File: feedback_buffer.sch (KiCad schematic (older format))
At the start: 20 parts

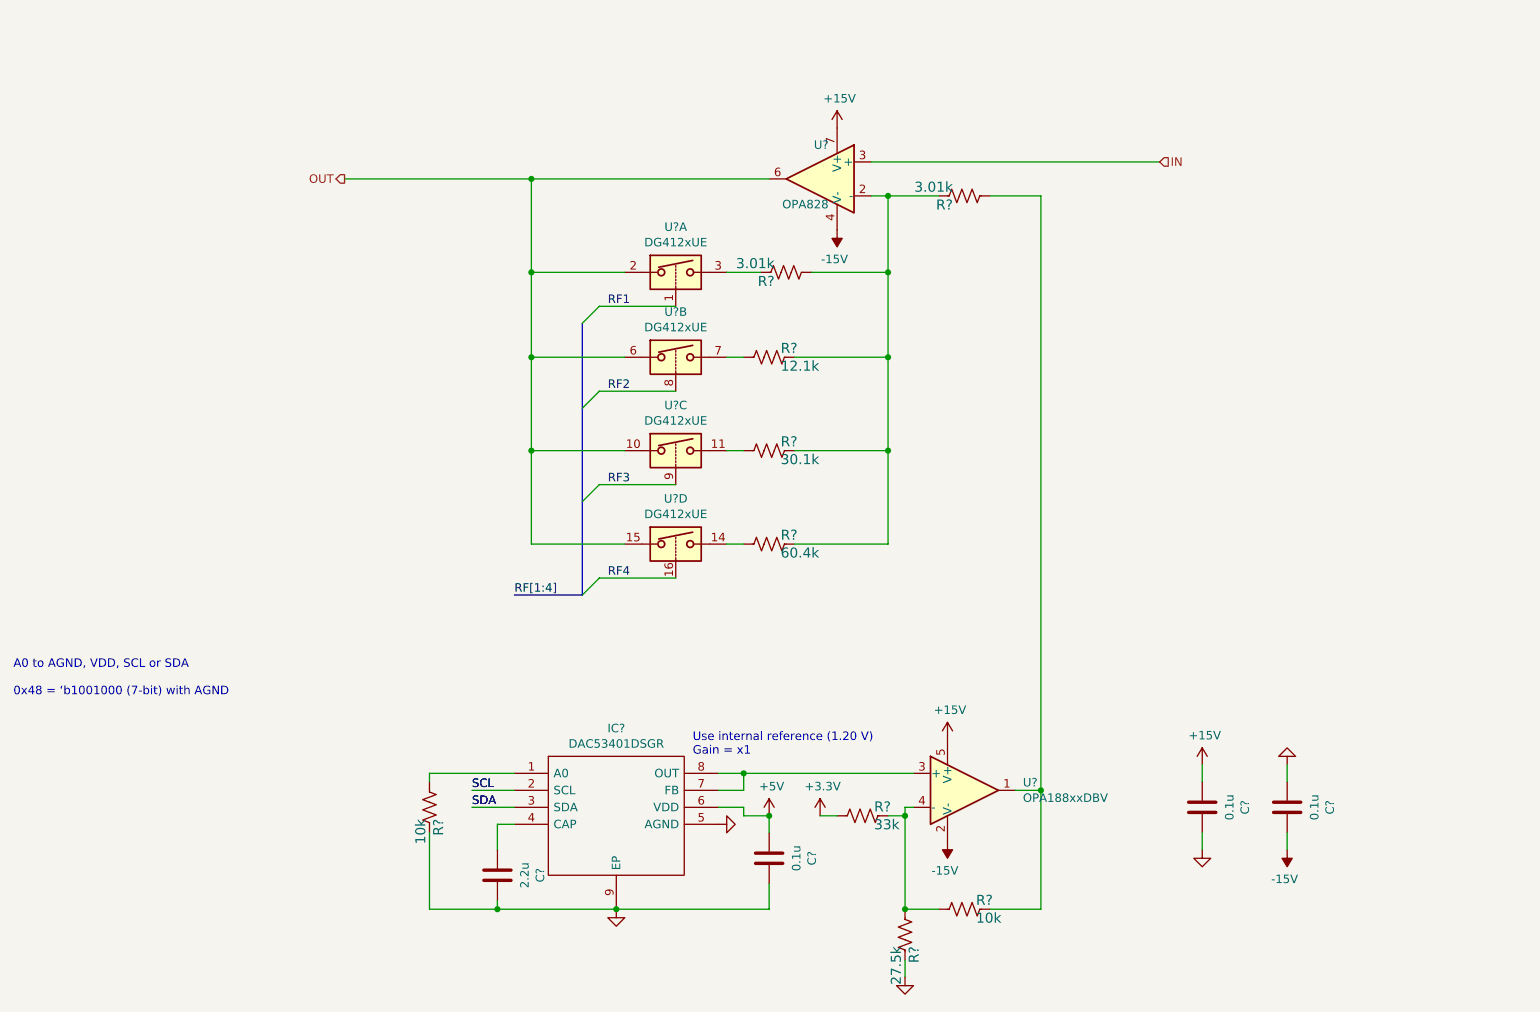
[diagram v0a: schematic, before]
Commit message: reduced ERC to just 4 warnings
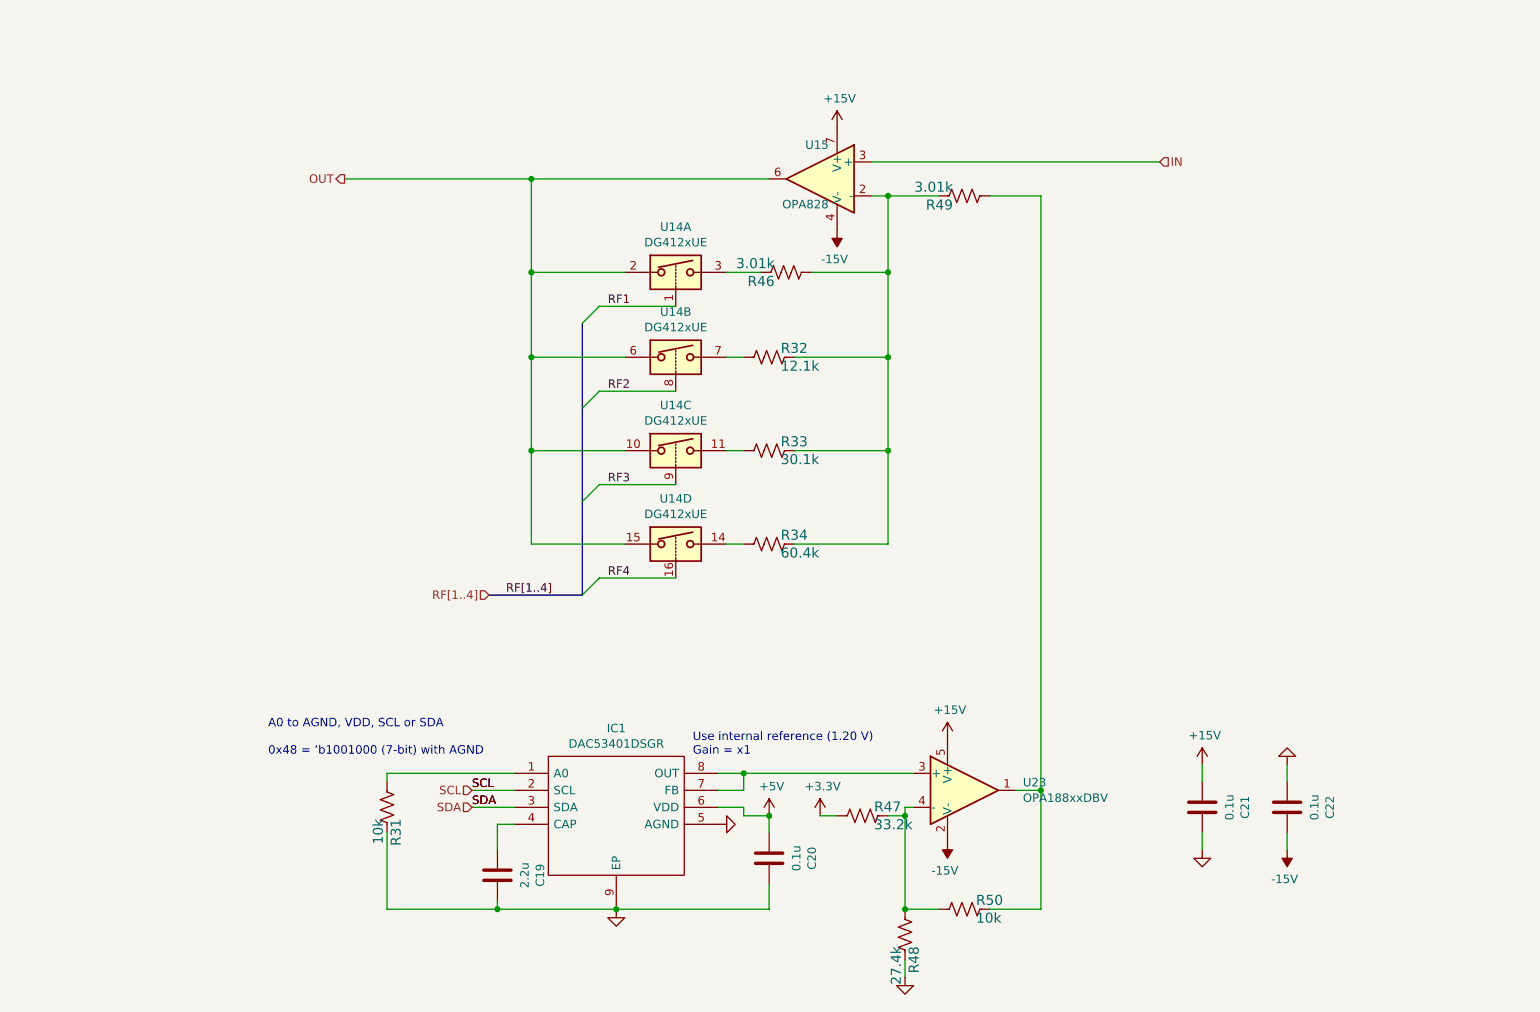
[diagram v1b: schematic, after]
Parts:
- R47: renamed from R?; value 33k -> 33.2k; Manf# (none) -> RC0603FR-0733K2L
- R48: renamed from R?; value 27.5k -> 27.4k; Manf# (none) -> RC0603FR-0727K4L
- R50: renamed from R?; Manf# (none) -> RC0603FR-0710KL
- gave numbers to parts that had none: 14
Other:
- moved on the sheet: R31

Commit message: updates to pcb layout
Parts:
- added C23, C24, C25, C26: DNI, Capacitor_SMD:C_0603_1608Metric, symbol Device:C
- IC1: footprint SON50P200X200X80-9N -> covg-kicad:SON50P200X200X80-9N
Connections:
- net at R32.1, R33.1, R34.1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: now also C23.1, C24.1, C25.1, C26.1
- net at R46.1, U14.3: now also C23.2
- net at R32.2, U14.7: now also C24.2
- net at R33.2, U14.11: now also C25.2
- net at R34.2, U14.14: now also C26.2
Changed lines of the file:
@@
 $EndComp
 Wire Wire Line
-	5450 2050 5250 2050
-Wire Wire Line
-	5750 2050 6200 2050
+	5750 2050 5850 2050
 Wire Wire Line
 	6200 2050 6200 1600
@@
 F 0 "IC1" H 4600 5265 50  0000 C CNN
 F 1 "DAC53401DSGR" H 4600 5174 50  0000 C CNN
-F 2 "SON50P200X200X80-9N" H 5050 5100 50  0001 L CNN
+F 2 "covg-kicad:SON50P200X200X80-9N" H 5050 5100 50  0001 L CNN
 F 3 "http://www.ti.com/lit/ds/symlink/dac53401.pdf?HQS=TI-null-null-digikeymode-df-pf-null-wwe&ts=1589734386977" H 5050 5000 50  0001 L CNN
 F 4 "Digital to Analog Converters - DAC 10-bit 1-channel DAC with NVM, buffered voltage output and I2C interface 8-WSON -40 to 125" H 5050 4900 50  0001 L CNN "Description"
@@
 Connection ~ 4100 2550
 Wire Wire Line
-	4650 3650 4100 3650
-Wire Wire Line
 	4100 3650 4100 3100
 Connection ~ 4100 3100
@@
 $EndComp
 Wire Wire Line
-	5650 2550 6200 2550
+	5650 2550 5850 2550
 Wire Wire Line
 	6200 2550 6200 2050
 Connection ~ 6200 2050
 Wire Wire Line
-	5650 3100 6200 3100
+	5650 3100 5850 3100
 Wire Wire Line
 	6200 3100 6200 2550
 Connection ~ 6200 2550
 Wire Wire Line
-	5650 3650 6200 3650
+	5650 3650 5850 3650
 Wire Wire Line
 	6200 3650 6200 3100
 Connection ~ 6200 3100
 Wire Wire Line
-	5350 3100 5250 3100
-Wire Wire Line
-	5350 3650 5250 3650
-Wire Wire Line
-	5350 2550 5250 2550
+	5350 3100 5300 3100
+Wire Wire Line
+	5350 3650 5300 3650
+Wire Wire Line
+	5350 2550 5300 2550
 $Comp
 L Device:R_US R?
@@
 Text HLabel 3000 1500 0    50   Output ~ 0
 OUT
-Wire Wire Line
-	4950 3850 4500 3850
 Text Label 4550 2250 0    50   ~ 0
 RF1
@@
 Wire Wire Line
 	3250 5000 3250 5050
+$Comp
+L Device:C C?
+U 1 1 6274A814
+P 5550 2350
+AR Path="/6032F251/6274A814" Ref="C?"  Part="1"
+AR Path="/6032F251/608FDC40/6274A814" Ref="C?"  Part="1"
+AR Path="/6032F251/62017813/6274A814" Ref="C23"  Part="1"
+F 0 "C23" V 5450 2200 50  0000 C CNN
+F 1 "DNI" V 5450 2500 50  0000 C CNN
+F 2 "Capacitor_SMD:C_0603_1608Metric" H 5588 2200 50  0001 C CNN
+F 3 "~" H 5550 2350 50  0001 C CNN
+F 4 "" H 5298 2450 50  0001 C CNN "Manf#"
+F 5 "20%" H 5298 2450 50  0001 C CNN "Tolerance"
+F 6 "25V" H 5298 2450 50  0001 C CNN "voltage"
+	1    5550 2350
+	0    1    1    0
+$EndComp
+$Comp
+L Device:C C?
+U 1 1 6275089B
+P 5550 2850
+AR Path="/6032F251/6275089B" Ref="C?"  Part="1"
+AR Path="/6032F251/608FDC40/6275089B" Ref="C?"  Part="1"
+AR Path="/6032F251/62017813/6275089B" Ref="C24"  Part="1"
+F 0 "C24" V 5450 2700 50  0000 C CNN
+F 1 "DNI" V 5450 3000 50  0000 C CNN
+F 2 "Capacitor_SMD:C_0603_1608Metric" H 5588 2700 50  0001 C CNN
+F 3 "~" H 5550 2850 50  0001 C CNN
+F 4 "" H 5298 2950 50  0001 C CNN "Manf#"
+F 5 "20%" H 5298 2950 50  0001 C CNN "Tolerance"
+F 6 "25V" H 5298 2950 50  0001 C CNN "voltage"
+	1    5550 2850
+	0    1    1    0
+$EndComp
+$Comp
+L Device:C C?
+U 1 1 62750F44
+P 5550 3400
+AR Path="/6032F251/62750F44" Ref="C?"  Part="1"
+AR Path="/6032F251/608FDC40/62750F44" Ref="C?"  Part="1"
+AR Path="/6032F251/62017813/62750F44" Ref="C25"  Part="1"
+F 0 "C25" V 5450 3250 50  0000 C CNN
+F 1 "DNI" V 5450 3550 50  0000 C CNN
+F 2 "Capacitor_SMD:C_0603_1608Metric" H 5588 3250 50  0001 C CNN
+F 3 "~" H 5550 3400 50  0001 C CNN
+F 4 "" H 5298 3500 50  0001 C CNN "Manf#"
+F 5 "20%" H 5298 3500 50  0001 C CNN "Tolerance"
+F 6 "25V" H 5298 3500 50  0001 C CNN "voltage"
+	1    5550 3400
+	0    1    1    0
+$EndComp
+$Comp
+L Device:C C?
+U 1 1 62751479
+P 5550 3950
+AR Path="/6032F251/62751479" Ref="C?"  Part="1"
+AR Path="/6032F251/608FDC40/62751479" Ref="C?"  Part="1"
+AR Path="/6032F251/62017813/62751479" Ref="C26"  Part="1"
+F 0 "C26" V 5450 3800 50  0000 C CNN
+F 1 "DNI" V 5450 4100 50  0000 C CNN
+F 2 "Capacitor_SMD:C_0603_1608Metric" H 5588 3800 50  0001 C CNN
+F 3 "~" H 5550 3950 50  0001 C CNN
+F 4 "" H 5298 4050 50  0001 C CNN "Manf#"
+F 5 "20%" H 5298 4050 50  0001 C CNN "Tolerance"
+F 6 "25V" H 5298 4050 50  0001 C CNN "voltage"
+	1    5550 3950
+	0    1    1    0
+$EndComp
+Wire Wire Line
+	5700 2350 5850 2350
+Wire Wire Line
+	5850 2350 5850 2050
+Connection ~ 5850 2050
+Wire Wire Line
+	5850 2050 6200 2050
+Wire Wire Line
+	5400 2350 5300 2350
+Wire Wire Line
+	5300 2350 5300 2050
+Wire Wire Line
+	5250 2050 5300 2050
+Connection ~ 5300 2050
+Wire Wire Line
+	5300 2050 5450 2050
+Wire Wire Line
+	5400 2850 5300 2850
+Wire Wire Line
+	5300 2850 5300 2550
+Connection ~ 5300 2550
+Wire Wire Line
+	5300 2550 5250 2550
+Wire Wire Line
+	5700 2850 5850 2850
+Wire Wire Line
+	5850 2850 5850 2550
+Connection ~ 5850 2550
+Wire Wire Line
+	5850 2550 6200 2550
+Wire Wire Line
+	5400 3400 5300 3400
+Wire Wire Line
+	5300 3400 5300 3100
+Connection ~ 5300 3100
+Wire Wire Line
+	5300 3100 5250 3100
+Wire Wire Line
+	5700 3400 5850 3400
+Wire Wire Line
+	5850 3400 5850 3100
+Connection ~ 5850 3100
+Wire Wire Line
+	5850 3100 6200 3100
+Wire Wire Line
+	5400 3950 5300 3950
+Wire Wire Line
+	5300 3950 5300 3650
+Connection ~ 5300 3650
+Wire Wire Line
+	4950 3850 4500 3850
+Wire Wire Line
+	5250 3650 5300 3650
+Wire Wire Line
+	4650 3650 4100 3650
+Wire Wire Line
+	5700 3950 5850 3950
+Wire Wire Line
+	5850 3950 5850 3650
+Connection ~ 5850 3650
+Wire Wire Line
+	5850 3650 6200 3650
 Wire Bus Line
 	4400 2350 4400 3950

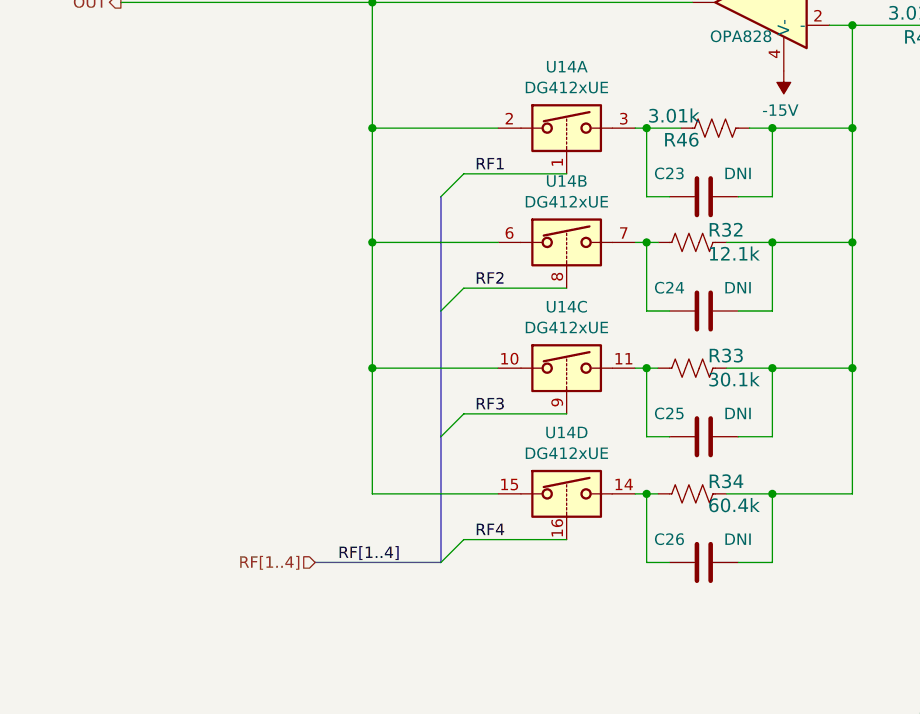
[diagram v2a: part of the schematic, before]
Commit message: updates to README
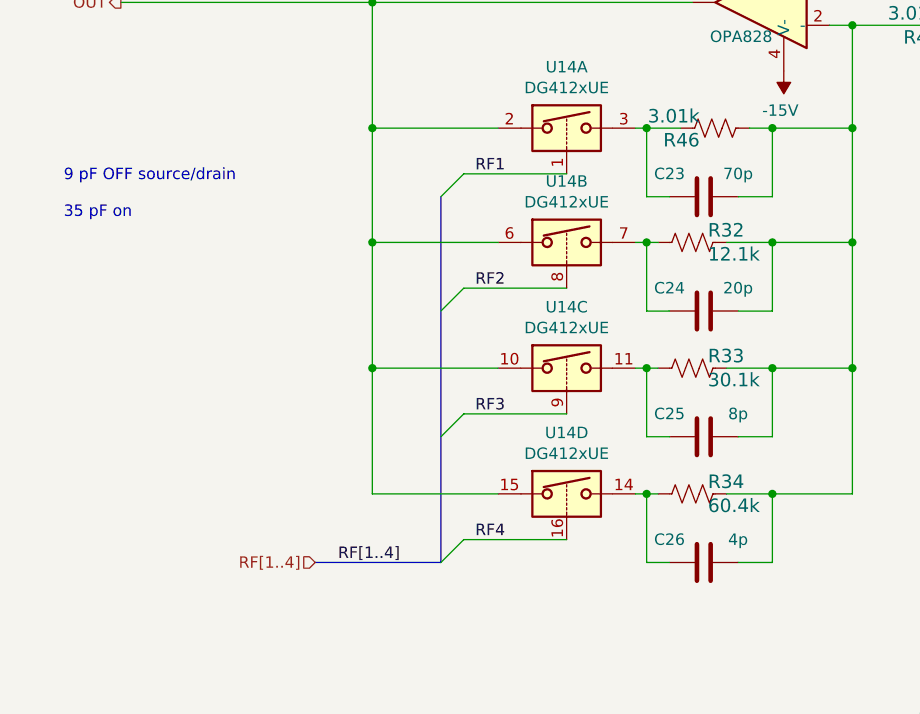
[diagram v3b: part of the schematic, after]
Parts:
- C23: value DNI -> 70p
- C24: value DNI -> 20p
- C25: value DNI -> 8p
- C26: value DNI -> 4p
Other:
- note added: "9 pF OFF source/drain\n\n35 pF on"
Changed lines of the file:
@@
 $Descr A4 11693 8268
 encoding utf-8
-Sheet 5 6
+Sheet 4 6
 Title ""
 Date ""
@@
 AR Path="/6032F251/62017813/6274A814" Ref="C23"  Part="1"
 F 0 "C23" V 5450 2200 50  0000 C CNN
-F 1 "DNI" V 5450 2500 50  0000 C CNN
+F 1 "70p" V 5450 2500 50  0000 C CNN
 F 2 "Capacitor_SMD:C_0603_1608Metric" H 5588 2200 50  0001 C CNN
 F 3 "~" H 5550 2350 50  0001 C CNN
@@
 AR Path="/6032F251/62017813/6275089B" Ref="C24"  Part="1"
 F 0 "C24" V 5450 2700 50  0000 C CNN
-F 1 "DNI" V 5450 3000 50  0000 C CNN
+F 1 "20p" V 5450 3000 50  0000 C CNN
 F 2 "Capacitor_SMD:C_0603_1608Metric" H 5588 2700 50  0001 C CNN
 F 3 "~" H 5550 2850 50  0001 C CNN
@@
 AR Path="/6032F251/62017813/62750F44" Ref="C25"  Part="1"
 F 0 "C25" V 5450 3250 50  0000 C CNN
-F 1 "DNI" V 5450 3550 50  0000 C CNN
+F 1 "8p" V 5450 3550 50  0000 C CNN
 F 2 "Capacitor_SMD:C_0603_1608Metric" H 5588 3250 50  0001 C CNN
 F 3 "~" H 5550 3400 50  0001 C CNN
@@
 AR Path="/6032F251/62017813/62751479" Ref="C26"  Part="1"
 F 0 "C26" V 5450 3800 50  0000 C CNN
-F 1 "DNI" V 5450 4100 50  0000 C CNN
+F 1 "4p" V 5450 4100 50  0000 C CNN
 F 2 "Capacitor_SMD:C_0603_1608Metric" H 5588 3800 50  0001 C CNN
 F 3 "~" H 5550 3950 50  0001 C CNN
@@
 Wire Bus Line
 	4400 2350 4400 3950
+Text Notes 2750 2450 0    50   ~ 0
+9 pF OFF source/drain\n\n35 pF on
 $EndSCHEMATC

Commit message: layout updates; part positioning
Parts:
- IC1: footprint covg-kicad:SON50P200X200X80-9N -> covg-kicad:WSON-8-1EP_2x2mm_P0.5mm_EP0.9x1.6mm_posMask
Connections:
- net GND: now also R31.2; no longer R31.1
- net at C23.1, C24.1, C25.1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: now also R46.1; no longer R46.2
- net at IC1.1 (A0): now also R31.1; no longer R31.2
- net at C23.2, U14.3: now also R46.2; no longer R46.1
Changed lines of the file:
@@
 $EndComp
-Wire Wire Line
-	5750 2050 5850 2050
 Wire Wire Line
 	6200 2050 6200 1600
@@
 F 0 "IC1" H 4600 5265 50  0000 C CNN
 F 1 "DAC53401DSGR" H 4600 5174 50  0000 C CNN
-F 2 "covg-kicad:SON50P200X200X80-9N" H 5050 5100 50  0001 L CNN
+F 2 "covg-kicad:WSON-8-1EP_2x2mm_P0.5mm_EP0.9x1.6mm_posMask" H 5050 5100 50  0001 L CNN
 F 3 "http://www.ti.com/lit/ds/symlink/dac53401.pdf?HQS=TI-null-null-digikeymode-df-pf-null-wwe&ts=1589734386977" H 5050 5000 50  0001 L CNN
 F 4 "Digital to Analog Converters - DAC 10-bit 1-channel DAC with NVM, buffered voltage output and I2C interface 8-WSON -40 to 125" H 5050 4900 50  0001 L CNN "Description"
@@
 F 5 "5%" H 3250 5200 50  0001 C CNN "Tolerance"
 	1    3250 5200
-	-1   0    0    1
+	1    0    0    -1
 $EndComp
 Wire Wire Line
 	3900 5800 3250 5800
-Wire Wire Line
-	3250 5800 3250 5350
 Connection ~ 3900 5800
 Text Notes 2550 4900 0    50   ~ 0
@@
 AR Path="/6032F251/621CE5F6" Ref="R?"  Part="1"
 AR Path="/6032F251/62017813/621CE5F6" Ref="R46"  Part="1"
-F 0 "R46" V 5547 2118 59  0000 L CNN
+F 0 "R46" V 5550 1800 59  0000 L CNN
 F 1 "3.01k" V 5652 2118 59  0000 L CNN
 F 2 "Resistor_SMD:R_0603_1608Metric" H 5600 2050 50  0001 C CNN
@@
 F 5 "1%" H 5600 2050 50  0001 C CNN "Tolerance"
 	1    5600 2050
-	0    -1   -1   0
+	0    1    1    0
 $EndComp
 Wire Wire Line
@@
 Text HLabel 3750 5200 0    50   Input ~ 0
 SDA
-Wire Wire Line
-	3250 5000 4000 5000
-Wire Wire Line
-	3250 5000 3250 5050
 $Comp
 L Device:C C?
@@
 Wire Wire Line
 	5850 2350 5850 2050
-Connection ~ 5850 2050
 Wire Wire Line
 	5850 2050 6200 2050
@@
 Wire Wire Line
 	5250 2050 5300 2050
-Connection ~ 5300 2050
-Wire Wire Line
-	5300 2050 5450 2050
 Wire Wire Line
 	5400 2850 5300 2850
@@
 Text Notes 2750 2450 0    50   ~ 0
 9 pF OFF source/drain\n\n35 pF on
+Wire Wire Line
+	5450 2050 5300 2050
+Connection ~ 5300 2050
+Wire Wire Line
+	5750 2050 5850 2050
+Connection ~ 5850 2050
+Wire Wire Line
+	3250 5050 3250 5000
+Wire Wire Line
+	3250 5000 4000 5000
+Wire Wire Line
+	3250 5350 3250 5800
 Wire Bus Line
 	4400 2350 4400 3950
